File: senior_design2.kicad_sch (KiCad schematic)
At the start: 21 parts

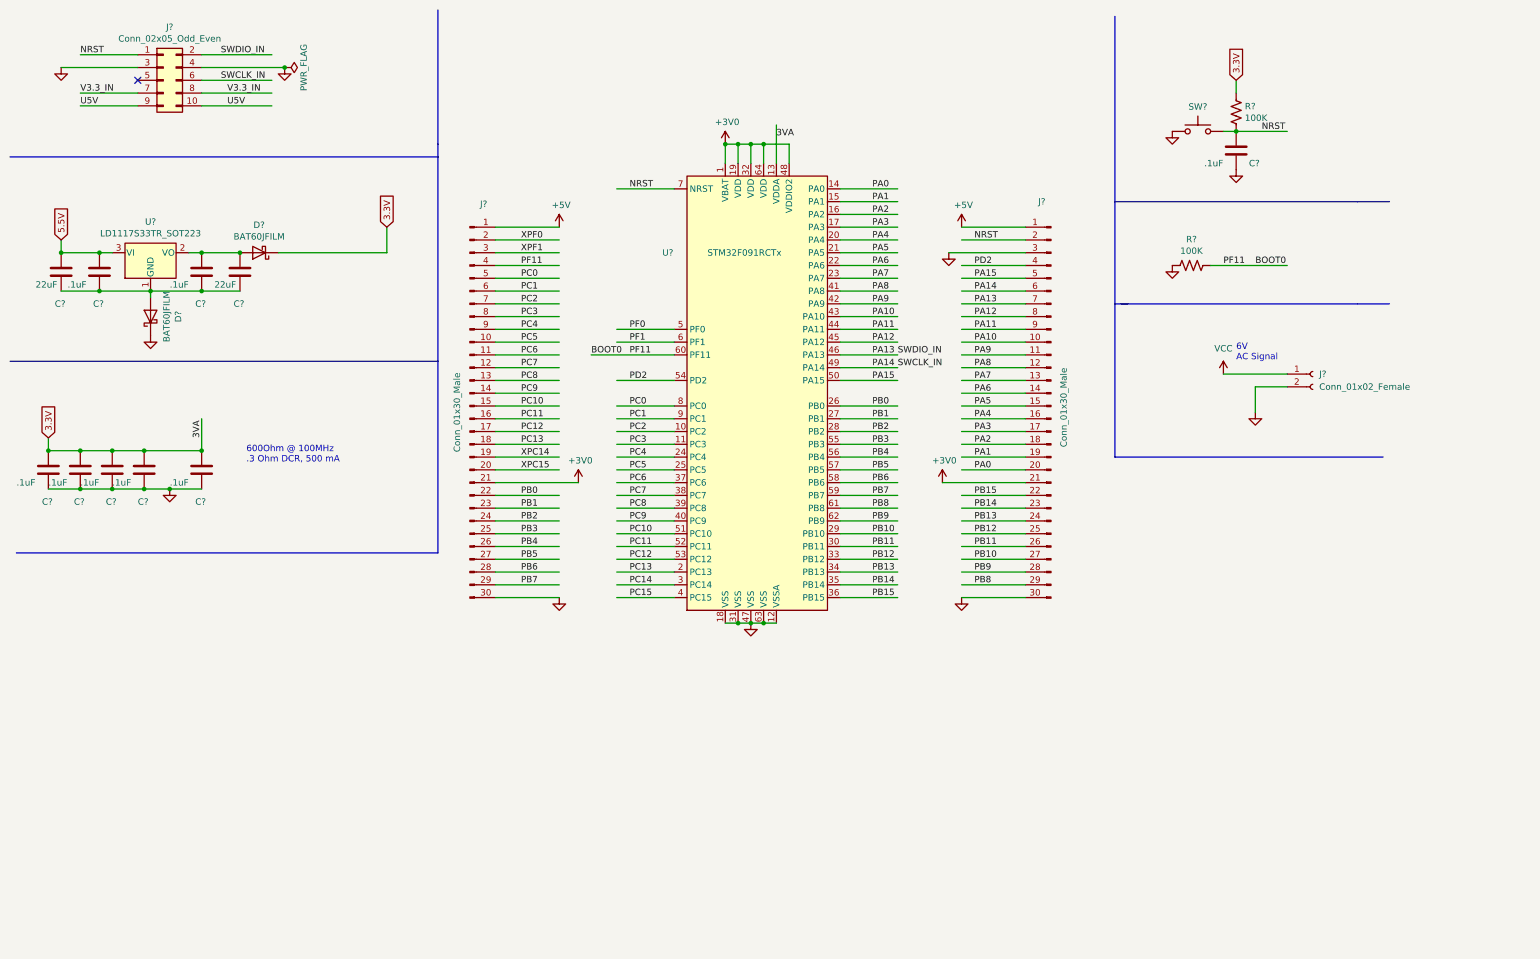
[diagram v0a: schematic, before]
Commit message: 2 new schematics (2 for Bluetooth without pins, 3 for Bluetooth with pins)
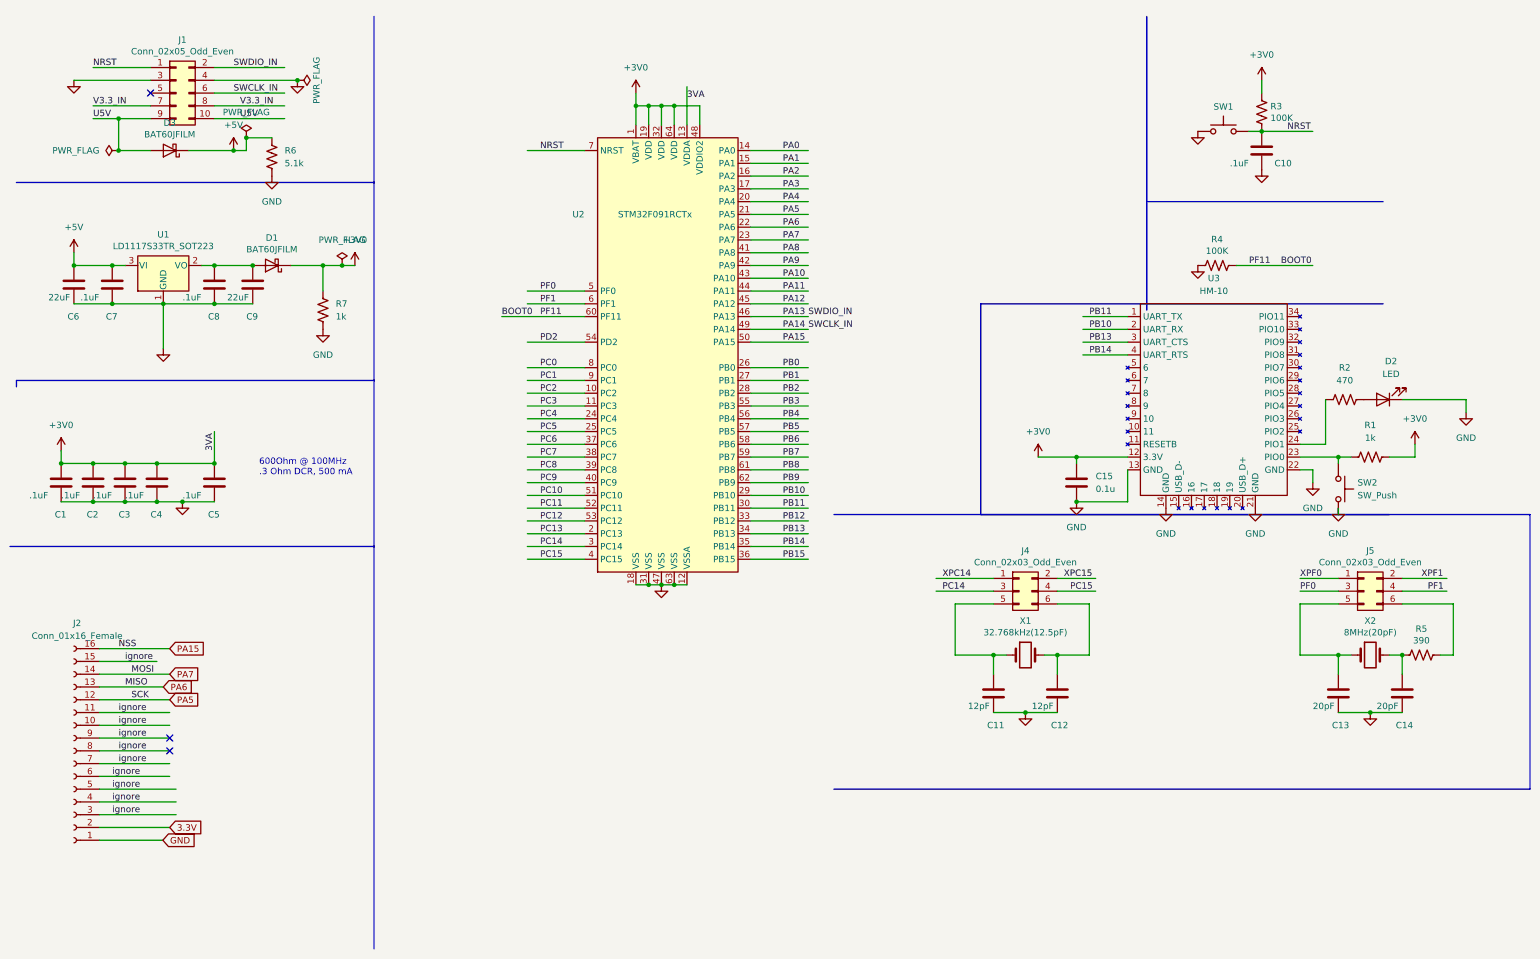
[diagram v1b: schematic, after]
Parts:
- removed C? (x8): .1uF, Capacitor_SMD:C_0805_2012Metric_Pad1.18x1.45mm_HandSolder, symbol Device:C
- removed C? (x2): 22uF, Capacitor_SMD:C_0805_2012Metric_Pad1.18x1.45mm_HandSolder, symbol Device:C
- removed D? (x2): BAT60JFILM, Diode_SMD:D_SOD-323, symbol Diode:BAT60A
- removed J? (x2): Conn_01x30_Male, local_models:HTSW-130-22-T-S, symbol Connector:Conn_01x30_Male
- removed J?: Conn_01x02_Female, local_models:J1, symbol Connector:Conn_01x02_Female
- removed J?: Conn_02x05_Odd_Even, Connector_IDC:IDC-Header_2x05_P2.54mm_Vertical, symbol Connector_Generic:Conn_02x05_Odd_Even
- removed R? (x2): 100K, Resistor_SMD:R_0805_2012Metric_Pad1.20x1.40mm_HandSolder, symbol Device:R_US
- removed SW?: SW_Push, Button_Switch_SMD:SW_SPST_PTS645, symbol Switch:SW_Push
- removed U?: STM32F091RCTx, Package_QFP:LQFP-64_10x10mm_P0.5mm, symbol MCU_ST_STM32F0:STM32F091RCTx
- removed U?: LD1117S33TR_SOT223, Package_TO_SOT_SMD:SOT-223-3_TabPin2, symbol Regulator_Linear:LD1117S33TR_SOT223
- added C1, C10, C2, C3, C4, C5, C7, C8: .1uF, Capacitor_SMD:C_0805_2012Metric_Pad1.18x1.45mm_HandSolder, symbol Device:C
- added C11, C12: 12pF, Capacitor_SMD:C_0805_2012Metric_Pad1.18x1.45mm_HandSolder, symbol Device:C
- added C13, C14: 20pF, Capacitor_SMD:C_0805_2012Metric_Pad1.18x1.45mm_HandSolder, symbol Device:C
- added C15: 0.1u, Capacitor_SMD:C_0805_2012Metric_Pad1.18x1.45mm_HandSolder, symbol Device:C
- added C6, C9: 22uF, Capacitor_SMD:C_0805_2012Metric_Pad1.18x1.45mm_HandSolder, symbol Device:C
- added D1, D3: BAT60JFILM, Diode_SMD:D_SOD-323, symbol Diode:BAT60A
- added D2: LED, LED_SMD:LED_0805_2012Metric, symbol Device:LED
- added J1: Conn_02x05_Odd_Even, Connector_IDC:IDC-Header_2x05_P2.54mm_Vertical, symbol Connector_Generic:Conn_02x05_Odd_Even
- added J2: Conn_01x16_Female, Connector_PinHeader_2.54mm:PinHeader_1x16_P2.54mm_Vertical, symbol Connector:Conn_01x16_Female
- added J4, J5: Conn_02x03_Odd_Even, Connector_PinHeader_1.27mm:PinHeader_2x03_P1.27mm_Vertical, symbol Connector_Generic:Conn_02x03_Odd_Even
- added R1, R7: 1k, Resistor_SMD:R_0805_2012Metric_Pad1.20x1.40mm_HandSolder, symbol Device:R_US
- added R2: 470, Resistor_SMD:R_0805_2012Metric_Pad1.20x1.40mm_HandSolder, symbol Device:R_US
- added R3, R4: 100K, Resistor_SMD:R_0805_2012Metric_Pad1.20x1.40mm_HandSolder, symbol Device:R_US
- added R5: 390, Resistor_SMD:R_0805_2012Metric_Pad1.20x1.40mm_HandSolder, symbol Device:R_US
- added R6: 5.1k, Resistor_SMD:R_0805_2012Metric_Pad1.20x1.40mm_HandSolder, symbol Device:R_US
- added SW1, SW2: SW_Push, Button_Switch_SMD:SW_SPST_PTS645, symbol Switch:SW_Push
- added U1: LD1117S33TR_SOT223, Package_TO_SOT_SMD:SOT-223-3_TabPin2, symbol Regulator_Linear:LD1117S33TR_SOT223
- added U2: STM32F091RCTx, Package_QFP:LQFP-64_10x10mm_P0.5mm, symbol MCU_ST_STM32F0:STM32F091RCTx
- added U3: HM-10, Library:HM-10, symbol New_Library_0:HM-10
- added X1: 32.768kHz(12.5pF), Crystal:Crystal_SMD_3225-4Pin_3.2x2.5mm, symbol Device:Crystal
- added X2: 8MHz(20pF), Crystal:Crystal_SMD_3225-4Pin_3.2x2.5mm, symbol Device:Crystal
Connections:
- net +3V0: now also C1.1, C15.1, C2.1, C3.1, C4.1, C5.1, D1.1 (K), R1.2, R3.1, R7.1, U2.1 (VBAT), U2.13 (VDDA), U2.19 (VDD), U2.32 (VDD), U2.48 (VDDIO2), U2.64 (VDD), U3.12 (3.3V)
- net +5V: now also C6.1, C7.1, D3.1 (K), R6.1, U1.3 (VI)
- net 3.3V: now also J2.2 (Pin_2)
- net BOOT0: now also R4.1, U2.60 (PF11)
- net GND: now also C1.2, C10.2, C11.2, C12.2, C13.2, C14.2, C15.2, C2.2, C3.2, C4.2, C5.2, C6.2, C7.2, C8.2, C9.2, D2.1 (K), J1.3 (Pin_3), J1.4 (Pin_4), J2.1 (Pin_1), R4.2, R6.2, R7.2, SW1.1, SW2.2, U1.1 (GND), U2.12 (VSSA), U2.18 (VSS), U2.31 (VSS), U2.47 (VSS), U2.63 (VSS), U3.13 (GND), U3.14 (GND), U3.21 (GND), U3.22 (GND)
- net NRST: now also C10.1, J1.1 (Pin_1), R3.2, SW1.2, U2.7 (NRST)
- net PA0: now also U2.14 (PA0)
- net PA1: now also U2.15 (PA1)
- net PA10: now also U2.43 (PA10)
- net PA11: now also U2.44 (PA11)
- net PA12: now also U2.45 (PA12)
- net PA13: now also J1.2 (Pin_2), U2.46 (PA13)
- net PA14: now also J1.6 (Pin_6), U2.49 (PA14)
- net PA15: now also J2.16 (Pin_16), U2.50 (PA15)
- net PA2: now also U2.16 (PA2)
- net PA3: now also U2.17 (PA3)
- net PA4: now also U2.20 (PA4)
- net PA5: now also J2.12 (Pin_12), U2.21 (PA5)
- net PA6: now also J2.13 (Pin_13), U2.22 (PA6)
- net PA7: now also J2.14 (Pin_14), U2.23 (PA7)
- net PA8: now also U2.41 (PA8)
- net PA9: now also U2.42 (PA9)
- net PB0: now also U2.26 (PB0)
- net PB1: now also U2.27 (PB1)
- net PB10: now also U2.29 (PB10), U3.2 (UART_RX)
- net PB11: now also U2.30 (PB11), U3.1 (UART_TX)
- net PB12: now also U2.33 (PB12)
- net PB13: now also U2.34 (PB13), U3.3 (UART_CTS)
- net PB14: now also U2.35 (PB14), U3.4 (UART_RTS)
- net PB15: now also U2.36 (PB15)
- net PB2: now also U2.28 (PB2)
- net PB3: now also U2.55 (PB3)
- net PB4: now also U2.56 (PB4)
- net PB5: now also U2.57 (PB5)
- net PB6: now also U2.58 (PB6)
- net PB7: now also U2.59 (PB7)
- net PB8: now also U2.61 (PB8)
- net PB9: now also U2.62 (PB9)
- net PC0: now also U2.8 (PC0)
- net PC1: now also U2.9 (PC1)
- net PC10: now also U2.51 (PC10)
- net PC11: now also U2.52 (PC11)
- net PC12: now also U2.53 (PC12)
- net PC13: now also U2.2 (PC13)
- net PC14: now also J4.3 (Pin_3), U2.3 (PC14)
- net PC15: now also J4.4 (Pin_4), U2.4 (PC15)
- net PC2: now also U2.10 (PC2)
- net PC3: now also U2.11 (PC3)
- net PC4: now also U2.24 (PC4)
- net PC5: now also U2.25 (PC5)
- net PC6: now also U2.37 (PC6)
- net PC7: now also U2.38 (PC7)
- net PC8: now also U2.39 (PC8)
- net PC9: now also U2.40 (PC9)
- net PD2: now also U2.54 (PD2)
- net PF0: now also J5.3 (Pin_3), U2.5 (PF0)
- net PF1: now also J5.4 (Pin_4), U2.6 (PF1)
- net U5V: now also D3.2 (A), J1.10 (Pin_10), J1.9 (Pin_9)
- net V3.3_IN: now also J1.7 (Pin_7), J1.8 (Pin_8)
- net XPC14: now also J4.1 (Pin_1)
- net XPC15: now also J4.2 (Pin_2)
- net XPF0: now also J5.1 (Pin_1)
- net XPF1: now also J5.2 (Pin_2)
- new net: C8.1, C9.1, D1.2 (A), U1.2 (VO)
- new net: D2.2 (A), R2.2
- new net: J5.6 (Pin_6), R5.1
- new net: C14.1, R5.2, X2.2
- new net: C13.1, J5.5 (Pin_5), X2.1
- new net: R1.1, SW2.1, U3.23 (PIO0)
- new net: R2.1, U3.24 (PIO1)
- new net: C11.1, J4.5 (Pin_5), X1.1
- new net: C12.1, J4.6 (Pin_6), X1.2
- new net ignore: J2.10 (Pin_10), J2.11 (Pin_11), J2.15 (Pin_15), J2.3 (Pin_3), J2.4 (Pin_4), J2.5 (Pin_5), J2.6 (Pin_6), J2.7 (Pin_7), J2.8 (Pin_8), J2.9 (Pin_9)
- no-connect marks 1 -> 3
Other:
- note removed: "6V AC Signal"
